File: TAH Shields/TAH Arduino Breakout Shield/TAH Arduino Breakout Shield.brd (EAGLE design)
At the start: 96.8 x 68 mm, 9 parts, among them M1 ARDUINO_R3_ICSP_NODIM

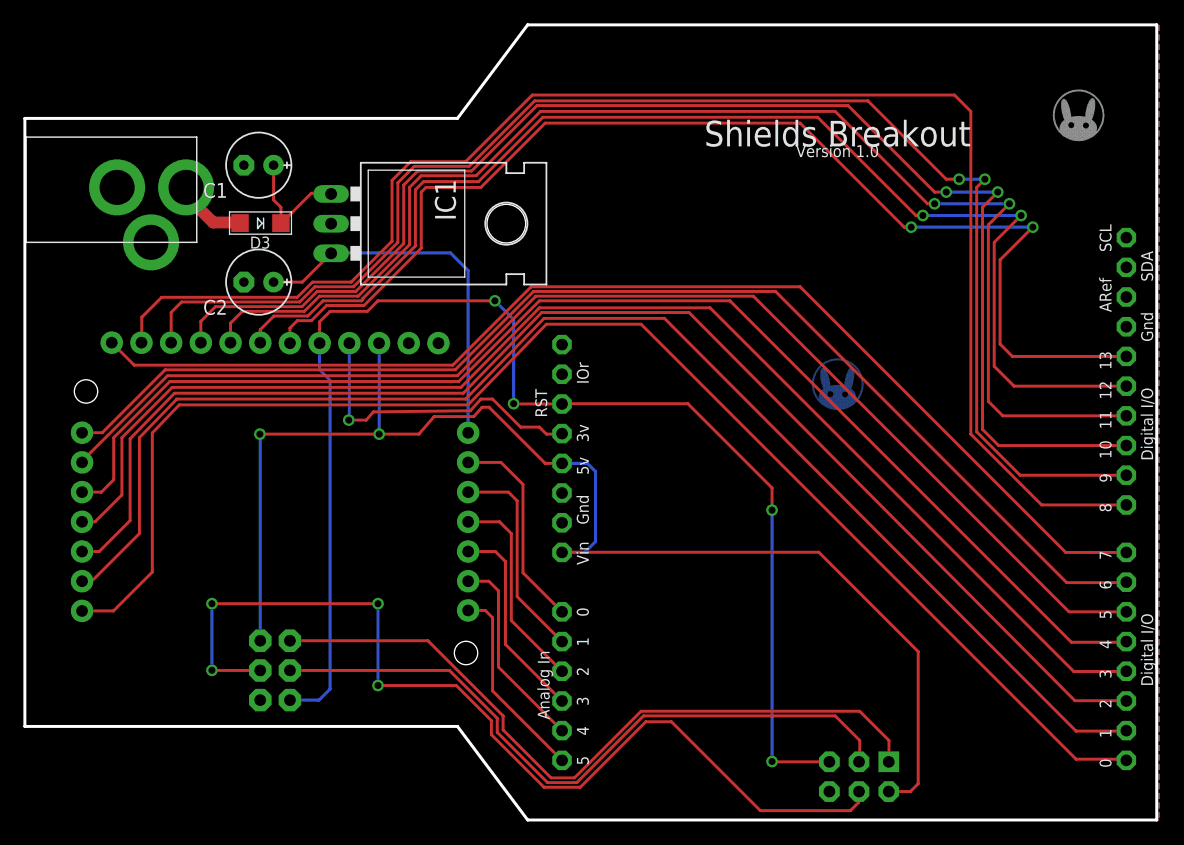
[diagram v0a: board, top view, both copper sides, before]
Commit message: All shields updated with latest Tah footprint
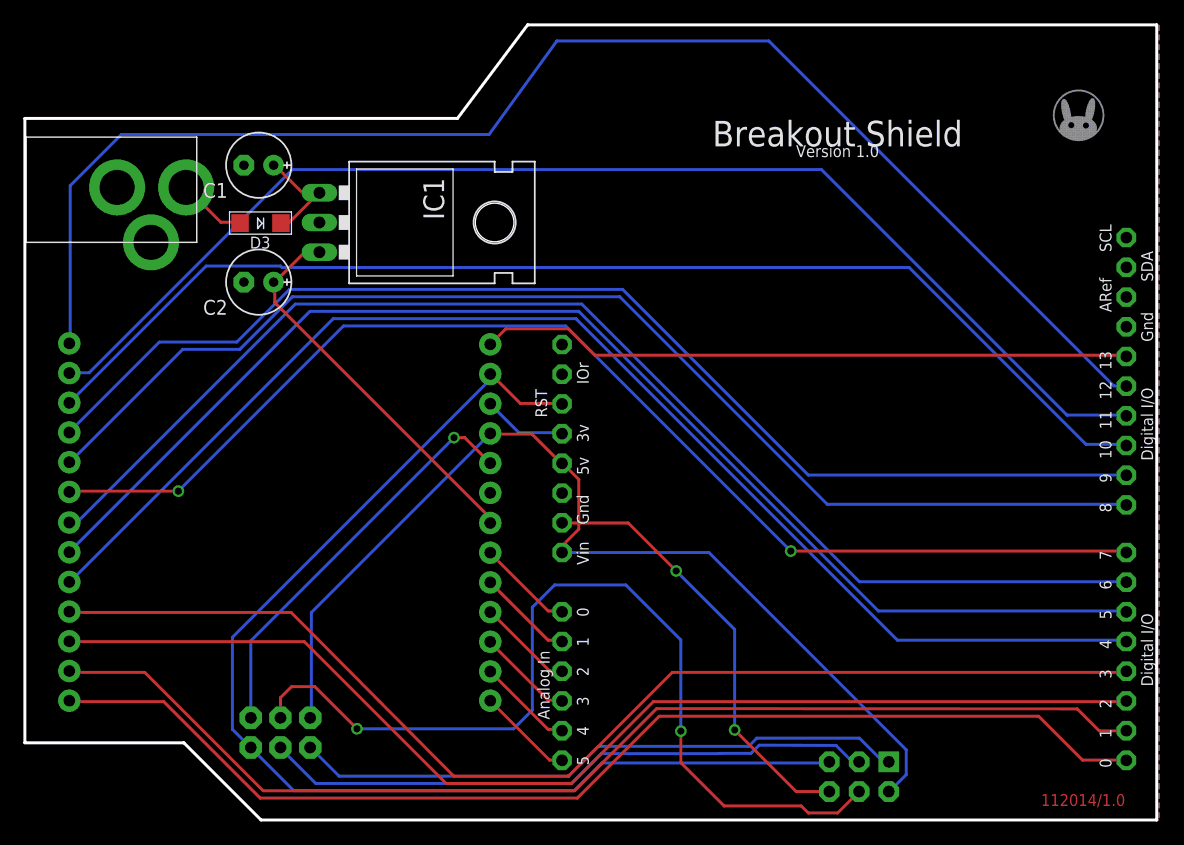
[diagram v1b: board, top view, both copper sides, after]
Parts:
- added U$5: (no value), TAH:TAH_PIN_FOOTPRINT_WITHOUT_ICSP_VERS1.0_SILK
- U$4: device TAH:TAH_LOGO_ETCHED -> TAH:TAHLOGO
- moved U$1 4.56 mm to (22.2, 23.6)
- moved IC1 1.00 mm to (29.0, 51.1)
- moved U$4 0.10 mm to (69.5, 37.2), flipped to the bottom
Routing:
- net GND: track 0.00 -> 72.6 mm, vias 0 -> 3
- net D13: track 101.3 -> 55.9 mm, vias 2 -> 0
- net 5V: track 114.8 -> 87.4 mm, vias 2 -> 0
- net D8: track 128.0 -> 103.6 mm
- net D0: track 122.0 -> 98.3 mm
- net D1: track 118.2 -> 98.3 mm
- net 3.3V: track 26.9 -> 7.22 mm, vias 1 -> 0
- net D9: track 121.7 -> 102.1 mm, vias 2 -> 0
- net D2: track 115.8 -> 98.3 mm
- net D12: track 106.0 -> 122.0 mm, vias 2 -> 0
- net D10: track 117.5 -> 101.6 mm, vias 2 -> 0
- net RESET: track 114.2 -> 101.0 mm, vias 4 -> 0
- net D3: track 112.7 -> 100.0 mm
- net A1: track 18.1 -> 8.25 mm
- net A0: track 17.8 -> 8.25 mm
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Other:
- outline, holes or cut-outs redrawn
- board text added: "112014/1.0"
- board text added: "Breakout Shield"
- board text added: "http://tah.io/start"
- board text removed: "Shields Breakout"
- board text removed: "http://www.tah.io/start"

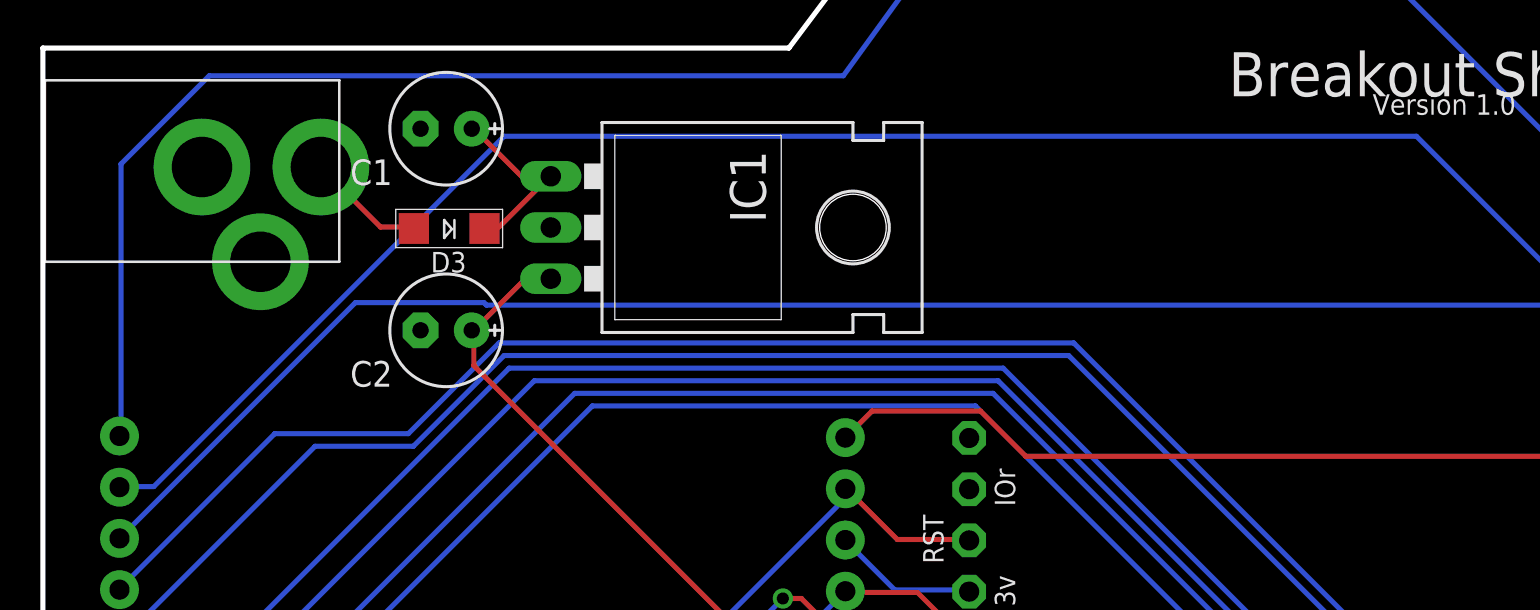
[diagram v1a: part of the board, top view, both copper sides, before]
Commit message: Silk Screen related minor changes
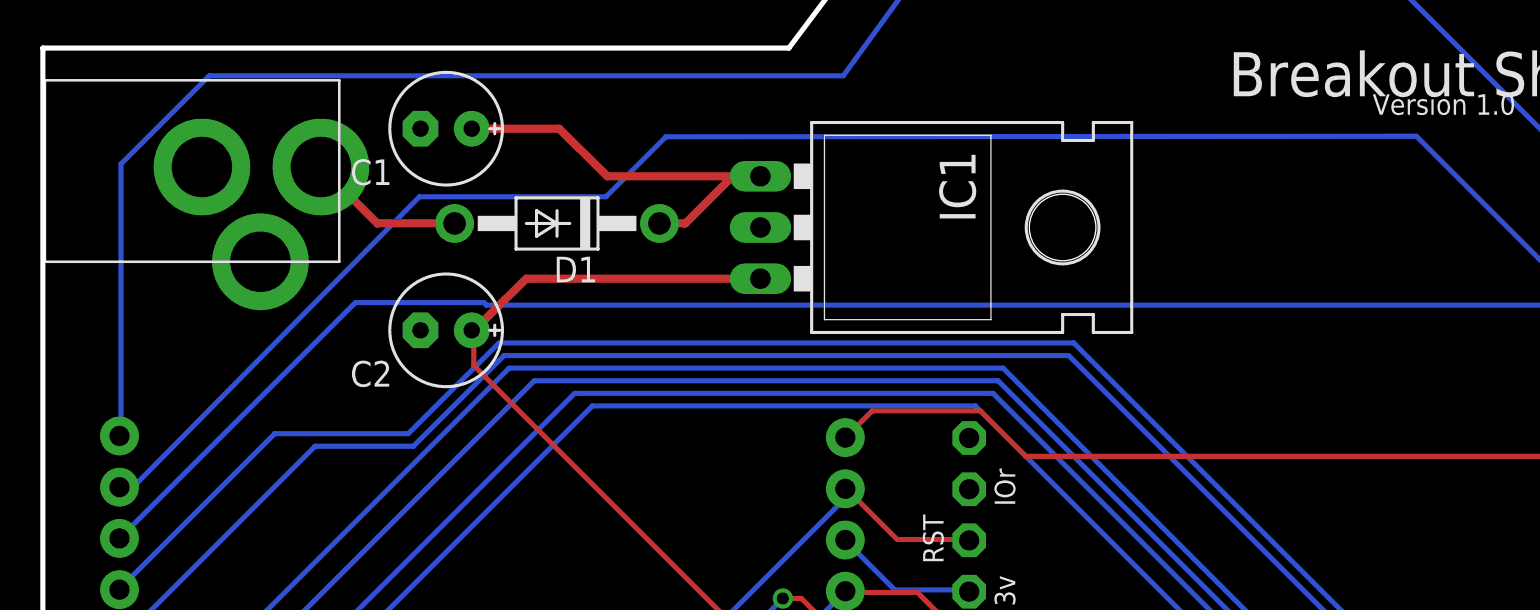
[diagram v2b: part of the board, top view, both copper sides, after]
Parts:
- removed D3: 1N4148, 1n4148 diode sot 23:SMADIODE
- added D1: 1N4004, adafruit:DO41-10
- U$5: device TAH:TAH_PIN_FOOTPRINT_WITHOUT_ICSP_VERS1.0_SILK -> TAH:TAH_SILK_FLIPPED
- moved IC1 10.4 mm to (39.4, 51.1)
- moved U$5 0.63 mm to (22.5, 25.5)
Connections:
- net N$4: now also D1.A; no longer D3.A
- net N$5: now also D1.C; no longer D3.C
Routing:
- net VIN: track 33.2 -> 43.6 mm
- net N$5: track 9.74 -> 19.9 mm
- net N$4: track 5.90 -> 7.79 mm
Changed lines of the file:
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@@
 <element name="U$1" library="TAH" package="TAH_PIN_FOOTPRINT_VER1.0" value="TAH_PIN_FOOTPRINT_VER1.0" x="22.25" y="23.63" rot="MR0"/>
 <element name="U$3" library="1n4148 diode sot 23" package="PJ-102A" value="2.1MMJACKTHM" x="4.5" y="54" rot="R90"/>
-<element name="IC1" library="SparkFun-PowerIC" package="TO-220-ALT" value="" x="29" y="51.1" rot="R270"/>
-<element name="D3" library="1n4148 diode sot 23" package="SMADIODE" value="1N4148" x="20" y="51" rot="R270"/>
+<element name="IC1" library="SparkFun-PowerIC" package="TO-220-ALT" value="" x="39.4" y="51.1" rot="R270"/>
 <element name="C1" library="Arduino Shield Pin Out" package="E2,5-6E" value="10uF" x="20" y="56" rot="R180"/>
 <element name="C2" library="Arduino Shield Pin Out" package="E2,5-6E" value="10uF" x="20" y="46" rot="R180"/>
@@
 <element name="M1" library="adafruit" package="ARDUINOR3_ICSP_NODIM" value="ARDUINO_R3_ICSP_NODIM" x="43.4" y="68.6" rot="R270"/>
 <element name="U$4" library="TAH" package="TAHLOGO" value="" x="69.5" y="37.2" rot="MR0"/>
-<element name="U$5" library="TAH" package="TAH_PIN_FOOTPRINT_WITHOUT_ICSP_VERS1.0_SILK" value="" x="21.9" y="25.3"/>
+<element name="U$5" library="TAH" package="TAH_SILK_FLIPPED" value="" x="22.5" y="25.5"/>
+<element name="D1" library="adafruit" package="DO41-10" value="1N4004" x="25.5" y="51.3" rot="R180"/>
 </elements>
 <signals>
@@
 <wire x1="89.125" y1="34.625" x2="94.125" y2="34.625" width="0.254" layer="16"/>
 <wire x1="68.125" y1="55.625" x2="89.125" y2="34.625" width="0.254" layer="16"/>
-<wire x1="22.875" y1="55.625" x2="68.125" y2="55.625" width="0.254" layer="16"/>
-<wire x1="5.5" y1="38.25" x2="22.875" y2="55.625" width="0.254" layer="16"/>
-<wire x1="3.875" y1="38.25" x2="5.5" y2="38.25" width="0.254" layer="16"/>
+<wire x1="18.675" y1="52.625" x2="27.925" y2="52.625" width="0.254" layer="16"/>
+<wire x1="27.925" y1="52.625" x2="30.9" y2="55.6" width="0.254" layer="16"/>
+<wire x1="30.9" y1="55.6" x2="68.125" y2="55.625" width="0.254" layer="16"/>
+<wire x1="4.5" y1="38.25" x2="18.675" y2="52.625" width="0.254" layer="16"/>
+<wire x1="3.875" y1="38.25" x2="4.5" y2="38.25" width="0.254" layer="16"/>
 <wire x1="94.125" y1="34.625" x2="94.2" y2="34.564" width="0.254" layer="16"/>
 <wire x1="3.875" y1="38.25" x2="3.8" y2="38.22" width="0.254" layer="16"/>
@@
 <contactref element="IC1" pad="OUT"/>
 <contactref element="U$1" pad="VIN"/>
-<wire x1="23.875" y1="48.5" x2="25.125" y2="48.5" width="0.254" layer="1"/>
-<wire x1="21.375" y1="46" x2="23.875" y2="48.5" width="0.254" layer="1"/>
-<wire x1="25.125" y1="48.5" x2="25.19" y2="48.56" width="0.254" layer="1"/>
+<wire x1="21.375" y1="46" x2="23.975" y2="48.56" width="0.4064" layer="1"/>
+<wire x1="23.975" y1="48.56" x2="35.59" y2="48.56" width="0.4064" layer="1"/>
 <wire x1="21.375" y1="46" x2="21.27" y2="46" width="0.254" layer="1"/>
 <wire x1="39.75" y1="25.875" x2="39.75" y2="25.5" width="0.254" layer="1"/>
@@
 <signal name="N$4">
 <contactref element="U$3" pad="TIP"/>
-<contactref element="D3" pad="A"/>
-<wire x1="16.75" y1="51.125" x2="18.375" y2="51.125" width="0.254" layer="1"/>
-<wire x1="13.875" y1="54" x2="16.75" y2="51.125" width="0.254" layer="1"/>
-<wire x1="18.375" y1="51.125" x2="18.4" y2="51.05" width="0.254" layer="1"/>
-<wire x1="13.875" y1="54" x2="13.79" y2="54.1" width="0.254" layer="1"/>
+<contactref element="D1" pad="A"/>
+<wire x1="20.42" y1="51.3" x2="16.59" y2="51.3" width="0.4064" layer="1"/>
+<wire x1="16.59" y1="51.3" x2="13.79" y2="54.1" width="0.4064" layer="1"/>
 </signal>
 <signal name="N$5">
-<contactref element="D3" pad="C"/>
 <contactref element="IC1" pad="IN"/>
 <contactref element="C1" pad="+"/>
-<wire x1="22.625" y1="51.125" x2="22" y2="51.125" width="0.254" layer="1"/>
-<wire x1="25.125" y1="53.625" x2="22.625" y2="51.125" width="0.254" layer="1"/>
-<wire x1="22" y1="51.125" x2="21.9" y2="51.05" width="0.254" layer="1"/>
-<wire x1="25.125" y1="53.625" x2="25.19" y2="53.64" width="0.254" layer="1"/>
-<wire x1="24.375" y1="53" x2="21.375" y2="56" width="0.254" layer="1"/>
-<wire x1="21.375" y1="56" x2="21.27" y2="56" width="0.254" layer="1"/>
-<wire x1="24.375" y1="53" x2="25.19" y2="53.64" width="0.254" layer="1"/>
+<wire x1="28" y1="53.64" x2="25.6" y2="56" width="0.4064" layer="1"/>
+<wire x1="25.6" y1="56" x2="21.27" y2="56" width="0.4064" layer="1"/>
+<wire x1="28" y1="53.64" x2="34.2" y2="53.64" width="0.4064" layer="1"/>
+<contactref element="D1" pad="C"/>
+<wire x1="34.2" y1="53.64" x2="35.59" y2="53.64" width="0.4064" layer="1"/>
+<wire x1="30.58" y1="51.3" x2="31.86" y2="51.3" width="0.4064" layer="1"/>
+<wire x1="31.86" y1="51.3" x2="34.2" y2="53.64" width="0.4064" layer="1"/>
 </signal>
 <signal name="SCK">

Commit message: silk screen related changes
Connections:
- net D2: now also M1.SDA
- net D3: now also M1.SCL
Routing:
- net D2: track 98.3 -> 184.4 mm, vias 0 -> 3
- net D3: track 100.0 -> 139.8 mm
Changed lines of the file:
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@@
 <wire x1="94.125" y1="10.125" x2="94.2" y2="10.18" width="0.254" layer="1"/>
 <wire x1="3.875" y1="15.25" x2="3.8" y2="15.28" width="0.254" layer="1"/>
+<contactref element="M1" pad="SDA"/>
+<wire x1="94.2" y1="47.264" x2="79.464" y2="47.264" width="0.254" layer="1"/>
+<wire x1="79.464" y1="47.264" x2="74.1" y2="41.9" width="0.254" layer="1"/>
+<via x="74.1" y="41.9" extent="1-16" drill="0.6" shape="octagon"/>
+<wire x1="74.1" y1="41.9" x2="70.1" y2="41.9" width="0.254" layer="16"/>
+<wire x1="70.1" y1="41.9" x2="65" y2="36.8" width="0.254" layer="16"/>
+<via x="65" y="36.8" extent="1-16" drill="0.6" shape="octagon"/>
+<wire x1="65" y1="36.8" x2="65" y2="27.4" width="0.254" layer="1"/>
+<wire x1="65" y1="27.4" x2="62" y2="24.4" width="0.254" layer="1"/>
+<wire x1="62" y1="24.4" x2="62" y2="23" width="0.254" layer="1"/>
+<wire x1="62" y1="23" x2="71.2" y2="13.8" width="0.254" layer="1"/>
+<via x="71.2" y="13.8" extent="1-16" drill="0.6" shape="octagon"/>
+<wire x1="71.2" y1="13.8" x2="84.625" y2="13.8" width="0.254" layer="16"/>
+<wire x1="84.625" y1="13.8" x2="88.7" y2="10.125" width="0.254" layer="16"/>
+<wire x1="88.7" y1="10.125" x2="94.145" y2="10.125" width="0.254" layer="16"/>
+<wire x1="94.145" y1="10.125" x2="94.2" y2="10.18" width="0.254" layer="16"/>
 </signal>
 <signal name="D3">
@@
 <wire x1="94.125" y1="12.625" x2="94.2" y2="12.72" width="0.254" layer="1"/>
 <wire x1="3.875" y1="17.75" x2="3.8" y2="17.82" width="0.254" layer="1"/>
+<contactref element="M1" pad="SCL"/>
+<wire x1="94.2" y1="49.804" x2="95.496" y2="49.804" width="0.254" layer="16"/>
+<wire x1="95.496" y1="49.804" x2="95.8" y2="49.5" width="0.254" layer="16"/>
+<wire x1="95.8" y1="49.5" x2="95.8" y2="13.2" width="0.254" layer="16"/>
+<wire x1="95.8" y1="13.2" x2="95.3" y2="12.7" width="0.254" layer="16"/>
+<wire x1="95.3" y1="12.7" x2="94.22" y2="12.7" width="0.254" layer="16"/>
+<wire x1="94.22" y1="12.7" x2="94.2" y2="12.72" width="0.254" layer="16"/>
 </signal>
 <signal name="D4">

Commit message: Updated production ready files for Tah and shields
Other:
- board text added: "122014/1.0"
- board text removed: "112014/1.0"
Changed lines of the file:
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@@
 <text x="69.5" y="32.5" size="1.016" layer="22" rot="MR0" align="center">http://tah.io/start</text>
 <text x="69.5" y="31" size="1.016" layer="22" font="vector" rot="MR0" align="center">Version 1.0</text>
-<text x="86.9" y="1.2" size="1.016" layer="1">112014/1.0</text>
+<text x="86.9" y="1.2" size="1.016" layer="1">122014/1.0</text>
 </plain>
 <attributes>

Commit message: latest file update
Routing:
- net GND: vias 3 -> 4
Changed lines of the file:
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@@
 <via x="55.7" y="21.3" extent="1-16" drill="0.6" shape="octagon"/>
 <wire x1="55.7" y1="21.3" x2="51.6" y2="25.4" width="0.254" layer="1"/>
-<wire x1="51.6" y1="25.4" x2="45.96" y2="25.4" width="0.254" layer="1"/>
-<wire x1="45.96" y1="25.4" x2="45.94" y2="25.42" width="0.254" layer="1"/>
+<wire x1="51.6" y1="25.4" x2="45.96" y2="25.4" width="0.254" layer="16"/>
+<wire x1="45.96" y1="25.4" x2="45.94" y2="25.42" width="0.254" layer="16"/>
+<via x="51.6" y="25.4" extent="1-16" drill="0.6" shape="octagon"/>
 </signal>
 <signal name="5V">
